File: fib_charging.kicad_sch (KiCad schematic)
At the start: 0 parts

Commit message: added several ICs, implementted schematics for charger, boost converter and LDOs
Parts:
- added C1, C12, C2, C3, C8: 0.1uF, symbol Device:C_Small
- added C10, C11, C13, C14, C15, C16, C17, C18, C19, C20, C4, C5, C9: 10uF, symbol Device:C_Small
- added C6, C7: 47nF, symbol Device:C_Small
- added D1, D2: BZT52Bxx, Diode_SMD:D_SOD-123F, symbol Diode:BZT52Bxx
- added D3: LED, symbol Device:LED
- added J5, J6: Conn_01x02, symbol Connector_Generic:Conn_01x02
- added L1: 1uH, symbol Device:L_Small
- added P2: USB_C_Plug_USB2.0, symbol Connector:USB_C_Plug_USB2.0
- added Q1, Q2, Q3, Q4: CSD17581Q3A, Package_SON:VSON-8_3.3x3.3mm_P0.65mm_NexFET, symbol Transistor_FET:CSD17581Q3A
- added R1, R2: 294R, symbol Device:R_Small
- added R10, R5: 127K, symbol Device:R_Small
- added R3: 10K, symbol Device:R_Small
- added R4: 6.04K, symbol Device:R_Small
- added R6: 100K, symbol Device:R_Small
- added R7: 100R, symbol Device:R_Small
- added R8: 5.24K, symbol Device:R_Small
- added R9: 30.31K, symbol Device:R_Small
- added TH1: 10K, symbol Device:Thermistor
- added U1: BQ25798RQMR, Fibel2:IBQ25798RQMR, symbol Fibel2:BQ25798RQMR
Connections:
- new net: D2.1 (K), Q3.4 (G), Q4.4 (G), R2.1
- new net: R2.2, U1.11 (ACDRV1)
- new net: C10.1, C11.1, C8.1, C9.1, U1.29 (PMID)
- new net: C20.1, U1.24 (SDRV)
- new net: R8.2, R9.2, TH1.1, U1.16 (TS)
- new net: D3.2 (A), R10.2
- new net: R4.1, U1.20 (PROG)
- new net: C3.1, C4.1, C5.1, Q2.5 (D), Q4.5 (D), U1.2 (VBUS), U1.3 (VBUS)
- new net: C1.1, J5.2 (Pin_2), Q1.5 (D), U1.8 (VAC2)
- new net: C18.1, C19.1, J6.1 (Pin_1), R7.1, U1.22 (BAT), U1.23 (BAT)
- new net: D2.2 (A), Q3.1 (S), Q3.2 (S), Q3.3 (S), Q4.1 (S), Q4.2 (S), Q4.3 (S)
- new net: D3.1 (K), U1.1 (STAT)
- new net: R1.2, U1.10 (ACDRV2)
- new net: R5.2, R6.1, U1.17 (ILIM_HIZ)
- new net: R7.2, U1.18 (BATP)
- new net: C7.2, U1.19 (BTST2)
- new net: C7.1, L1.1, U1.26 (SW2)
- new net: C6.2, L1.2, U1.28 (SW1)
- new net: C6.1, U1.4 (BTST1)
- new net: P2.A7 (D-), U1.6 (D+)
- new net: P2.A6 (D+), U1.7 (D-)
- new net: C2.1, P2.A4 (VBUS), P2.A9 (VBUS), P2.B4 (VBUS), P2.B9 (VBUS), Q3.5 (D), U1.9 (VAC1)
- new net: D1.1 (K), Q1.4 (G), Q2.4 (G), R1.1
- new net: D1.2 (A), Q1.1 (S), Q1.2 (S), Q1.3 (S), Q2.1 (S), Q2.2 (S), Q2.3 (S)
- new net: P2.A5 (CC), R3.2
- new net CHG_SCL: U1.14 (SCL)
- new net CHG_SDA: U1.15 (SDA)
- new net GND: C1.2, C10.2, C11.2, C12.2, C13.2, C14.2, C15.2, C16.2, C17.2, C18.2, C19.2, C2.2, C20.2, C3.2, C4.2, C5.2, C8.2, C9.2, J5.1 (Pin_1), J6.2 (Pin_2), P2.A1 (GND), P2.A12 (GND), P2.B1 (GND), P2.B12 (GND), P2.S1 (SHIELD), R3.1, R4.2, R6.2, R9.1, TH1.2, U1.27 (GND)
- new net REGN: R10.1, R5.1, R8.1, U1.5 (REGN)
- new net VCC: C12.1, C13.1, C14.1, C15.1, C16.1, C17.1, U1.25 (SYS)
- new net ~{CHG_CE}: U1.13 (~{CE})
- new net ~{CHG_INT}: U1.21 (~{INT})
- no-connect marks 0 -> 1
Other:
- note added: "BATT_CON"
- note added: "SOLAR_CON"

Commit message: added symbol&footprint for orin/sodimm, added a bunch of specs and docs, partially implemented audio, full steam ahead
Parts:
- C1, C10, C11, C12, C13, C14, C15, C16, C17, C18, C19, C2, C20, C3, C4, C5, C6, C7, C8, C9: footprint (none) -> Capacitor_SMD:C_0603_1608Metric
- J5, J6: footprint (none) -> Connector_JST:JST_EH_S2B-EH_1x02_P2.50mm_Horizontal
- R1, R10, R2, R3, R4, R5, R6, R7, R8, R9: footprint (none) -> Resistor_SMD:R_0603_1608Metric
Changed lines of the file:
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@@
 			)
 		)
-		(property "Footprint" ""
+		(property "Footprint" "Resistor_SMD:R_0603_1608Metric"
 			(at 83.82 67.31 0)
 			(effects
@@
 			)
 		)
-		(property "Footprint" ""
+		(property "Footprint" "Capacitor_SMD:C_0603_1608Metric"
 			(at 217.17 67.31 0)
 			(effects
@@
 			)
 		)
-		(property "Footprint" ""
+		(property "Footprint" "Capacitor_SMD:C_0603_1608Metric"
 			(at 196.85 67.31 0)
 			(effects
@@
 			)
 		)
-		(property "Footprint" ""
+		(property "Footprint" "Capacitor_SMD:C_0603_1608Metric"
 			(at 184.15 57.15 0)
 			(effects
@@
 			)
 		)
-		(property "Footprint" ""
+		(property "Footprint" "Resistor_SMD:R_0603_1608Metric"
 			(at 184.15 95.25 0)
 			(effects
@@
 			)
 		)
-		(property "Footprint" ""
+		(property "Footprint" "Resistor_SMD:R_0603_1608Metric"
 			(at 194.31 85.09 0)
 			(effects
@@
 			)
 		)
-		(property "Footprint" ""
+		(property "Footprint" "Resistor_SMD:R_0603_1608Metric"
 			(at 184.15 69.85 0)
 			(effects
@@
 			)
 		)
-		(property "Footprint" ""
+		(property "Footprint" "Capacitor_SMD:C_0603_1608Metric"
 			(at 109.22 49.53 0)
 			(effects
@@
 			)
 		)
-		(property "Footprint" ""
+		(property "Footprint" "Capacitor_SMD:C_0603_1608Metric"
 			(at 59.69 59.69 0)
 			(effects
@@
 			)
 		)
-		(property "Footprint" ""
+		(property "Footprint" "Connector_JST:JST_EH_S2B-EH_1x02_P2.50mm_Horizontal"
 			(at 228.6 49.53 0)
 			(effects
@@
 			)
 		)
-		(property "Footprint" ""
+		(property "Footprint" "Capacitor_SMD:C_0603_1608Metric"
 			(at 203.2 52.07 0)
 			(effects
@@
 			)
 		)
-		(property "Footprint" ""
+		(property "Footprint" "Capacitor_SMD:C_0603_1608Metric"
 			(at 246.38 92.71 0)
 			(effects
@@
 			)
 		)
-		(property "Footprint" ""
+		(property "Footprint" "Capacitor_SMD:C_0603_1608Metric"
 			(at 213.36 52.07 0)
 			(effects
@@
 			)
 		)
-		(property "Footprint" ""
+		(property "Footprint" "Capacitor_SMD:C_0603_1608Metric"
 			(at 129.54 49.53 0)
 			(effects
@@
 			)
 		)
-		(property "Footprint" ""
+		(property "Footprint" "Capacitor_SMD:C_0603_1608Metric"
 			(at 195.58 92.71 0)
 			(effects
@@
 			)
 		)
-		(property "Footprint" ""
+		(property "Footprint" "Capacitor_SMD:C_0603_1608Metric"
 			(at 226.06 92.71 0)
 			(effects
@@
 			)
 		)
-		(property "Footprint" ""
+		(property "Footprint" "Resistor_SMD:R_0603_1608Metric"
 			(at 54.61 88.9 0)
 			(effects
@@
 			)
 		)
-		(property "Footprint" ""
+		(property "Footprint" "Resistor_SMD:R_0603_1608Metric"
 			(at 186.69 78.74 0)
 			(effects
@@
 			)
 		)
-		(property "Footprint" ""
+		(property "Footprint" "Connector_JST:JST_EH_S2B-EH_1x02_P2.50mm_Horizontal"
 			(at 45.72 59.69 0)
 			(effects
@@
 			)
 		)
-		(property "Footprint" ""
+		(property "Footprint" "Capacitor_SMD:C_0603_1608Metric"
 			(at 119.38 49.53 0)
 			(effects
@@
 			)
 		)
-		(property "Footprint" ""
+		(property "Footprint" "Capacitor_SMD:C_0603_1608Metric"
 			(at 64.77 72.39 0)
 			(effects
@@
 			)
 		)
-		(property "Footprint" ""
+		(property "Footprint" "Capacitor_SMD:C_0603_1608Metric"
 			(at 125.73 95.25 0)
 			(effects
@@
 			)
 		)
-		(property "Footprint" ""
+		(property "Footprint" "Capacitor_SMD:C_0603_1608Metric"
 			(at 205.74 92.71 0)
 			(effects
@@
 			)
 		)
-		(property "Footprint" ""
+		(property "Footprint" "Resistor_SMD:R_0603_1608Metric"
 			(at 194.31 74.93 0)
 			(effects
@@
 			)
 		)
-		(property "Footprint" ""
+		(property "Footprint" "Capacitor_SMD:C_0603_1608Metric"
 			(at 236.22 92.71 0)
 			(effects
@@
 			)
 		)
-		(property "Footprint" ""
+		(property "Footprint" "Capacitor_SMD:C_0603_1608Metric"
 			(at 125.73 85.09 0)
 			(effects
@@
 			)
 		)
-		(property "Footprint" ""
+		(property "Footprint" "Capacitor_SMD:C_0603_1608Metric"
 			(at 207.01 67.31 0)
 			(effects
@@
 			)
 		)
-		(property "Footprint" ""
+		(property "Footprint" "Capacitor_SMD:C_0603_1608Metric"
 			(at 227.33 67.31 0)
 			(effects
@@
 			)
 		)
-		(property "Footprint" ""
+		(property "Footprint" "Capacitor_SMD:C_0603_1608Metric"
 			(at 215.9 92.71 0)
 			(effects
@@
 			)
 		)
-		(property "Footprint" ""
+		(property "Footprint" "Resistor_SMD:R_0603_1608Metric"
 			(at 185.42 52.07 0)
 			(effects
@@
 			)
 		)
-		(property "Footprint" ""
+		(property "Footprint" "Resistor_SMD:R_0603_1608Metric"
 			(at 184.15 102.87 0)
 			(effects
@@
 			)
 		)
-		(property "Footprint" ""
+		(property "Footprint" "Resistor_SMD:R_0603_1608Metric"
 			(at 83.82 59.69 0)
 			(effects

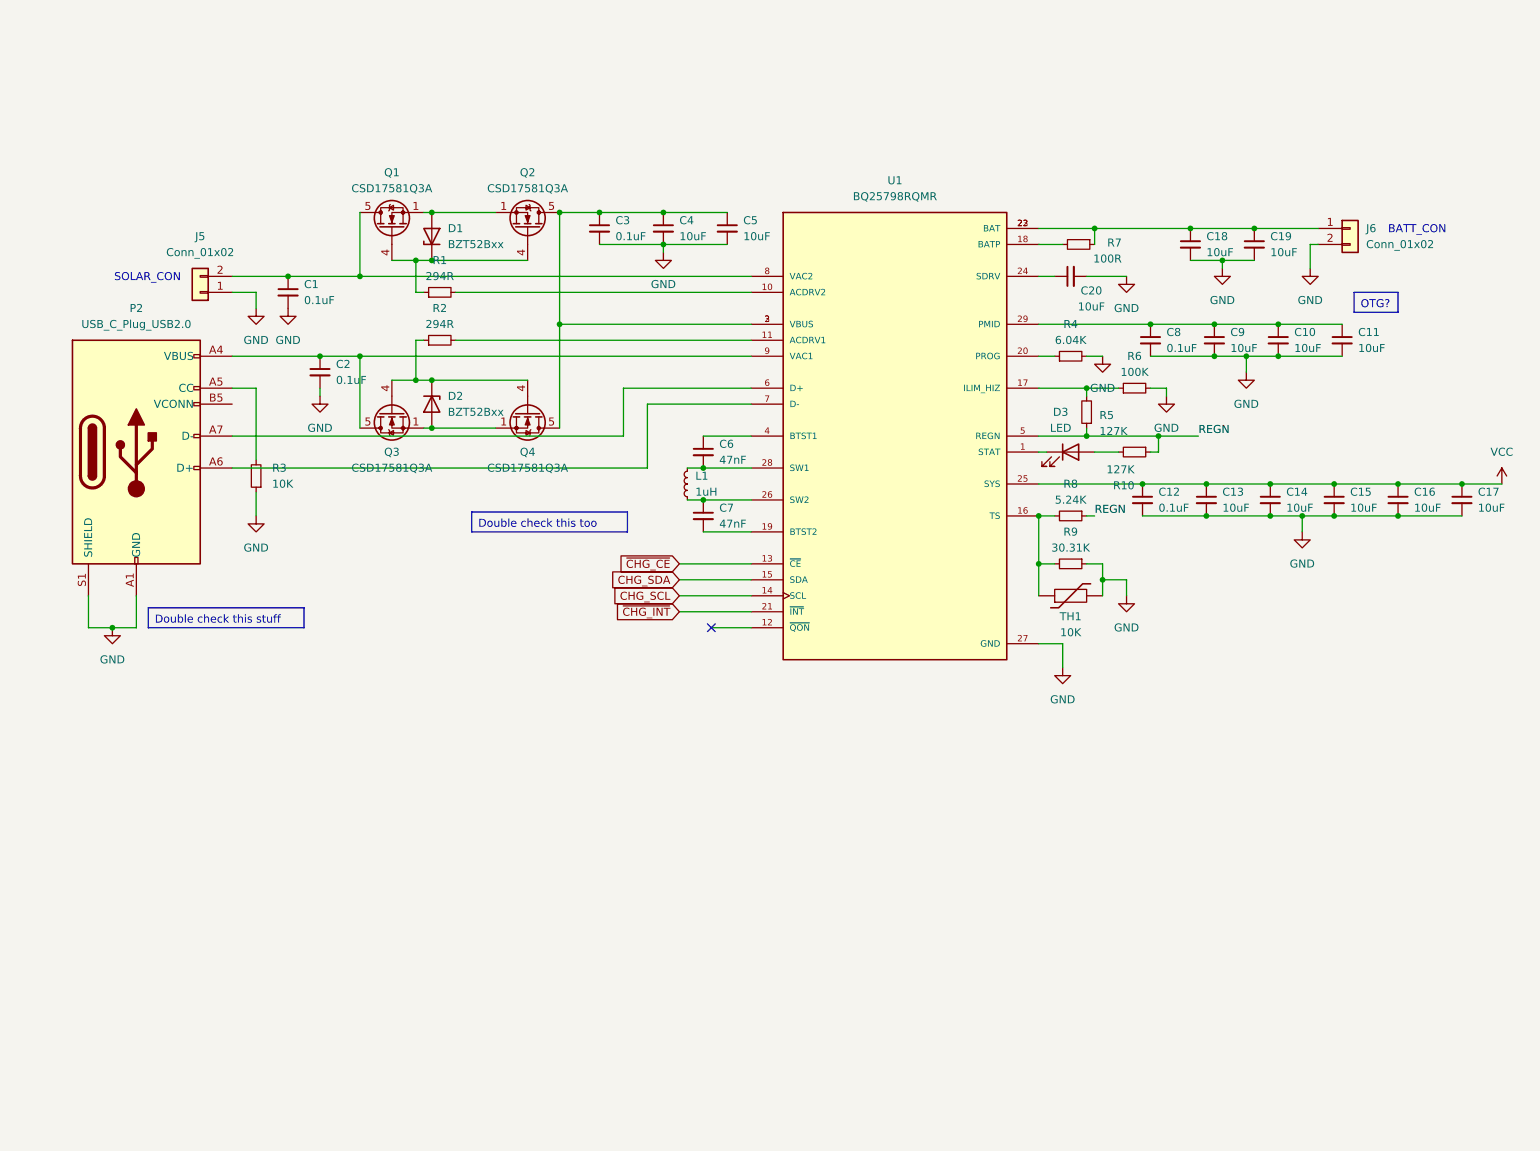
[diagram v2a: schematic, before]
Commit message: added usb+PD+DP & pcie implementations from antmicro design, added specs for USB components, rethought power+usb arch
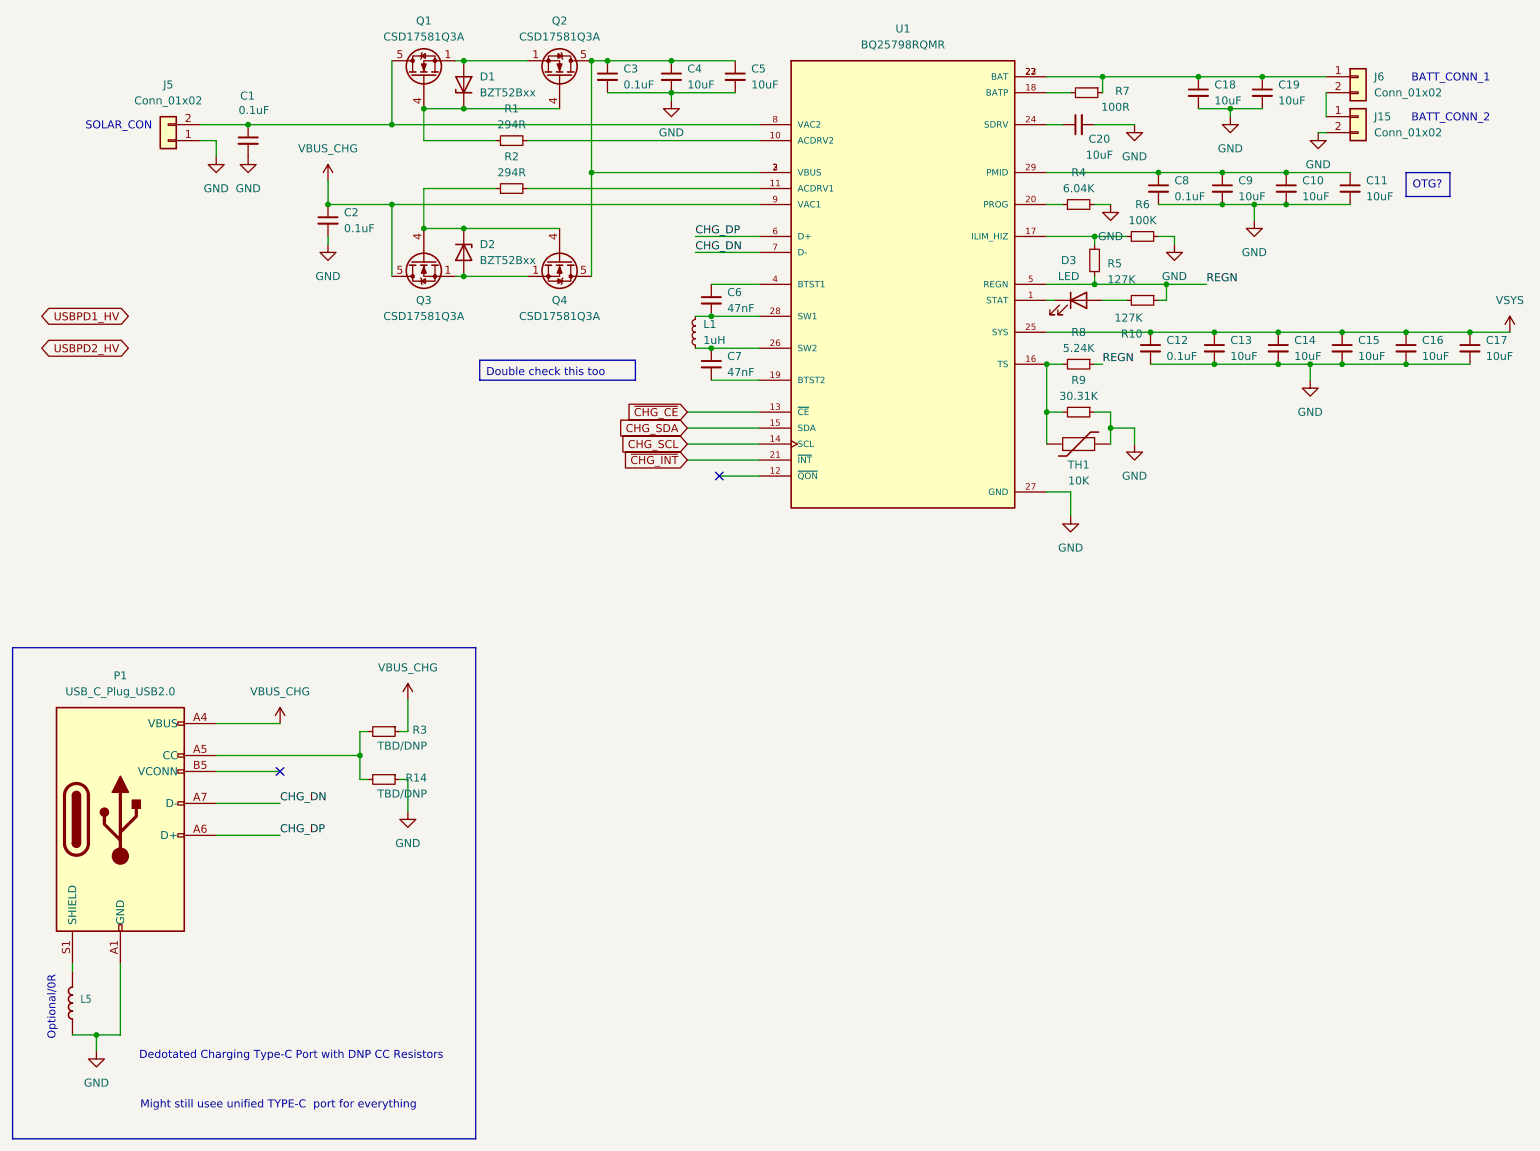
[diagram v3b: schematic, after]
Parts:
- removed P2: USB_C_Plug_USB2.0, symbol Connector:USB_C_Plug_USB2.0
- added J15: Conn_01x02, Connector_JST:JST_EH_S2B-EH_1x02_P2.50mm_Horizontal, symbol Connector_Generic:Conn_01x02
- added L5: ~, Untitled:L0603, symbol Untitled-eagle-import:INDUCTOR/FERRITE-BEAD'0603'
- added P1: USB_C_Plug_USB2.0, symbol Connector:USB_C_Plug_USB2.0
- added R14: TBD/DNP, Resistor_SMD:R_0603_1608Metric, symbol Device:R_Small
- R3: value 10K -> TBD/DNP
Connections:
- net GND: now also J15.2 (Pin_2), L5.1, P1.A1 (GND), P1.A12 (GND), P1.B1 (GND), P1.B12 (GND), R14.1; no longer J6.2 (Pin_2), R3.1
- net CHG_DP: now reaches U1.6 (D+)
- net CHG_DP: now also P1.A6 (D+)
- net CHG_DN: now reaches U1.7 (D-)
- net CHG_DN: now also P1.A7 (D-)
- net VBUS_CHG: now reaches C2.1, Q3.5 (D), U1.9 (VAC1)
- net VBUS_CHG: now also R3.1, P1.A4 (VBUS), P1.A9 (VBUS), P1.B4 (VBUS), P1.B9 (VBUS)
- net at R3.2: now also P1.A5 (CC), R14.2
- net VCC renamed VSYS
- new net: J15.1 (Pin_1), J6.2 (Pin_2)
- new net: L5.2, P1.S1 (SHIELD)
- no-connect marks 1 -> 2
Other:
- note added: "BATT_CONN_1"
- note added: "BATT_CONN_2"
- note added: "Dedotated Charging Type-C Port with DNP CC Resistors"
- note added: "Might still usee unified TYPE-C port for everything"
- note added: "Optional/0R"
- note removed: "BATT_CON"
- moved on the sheet: C1, C10, C11, C12, C13, C14, C15, C16, C17, C18, C19, C2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

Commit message: added nets for 40 pin headers (epd & rpi header) connected some of the nets i'm reeusing
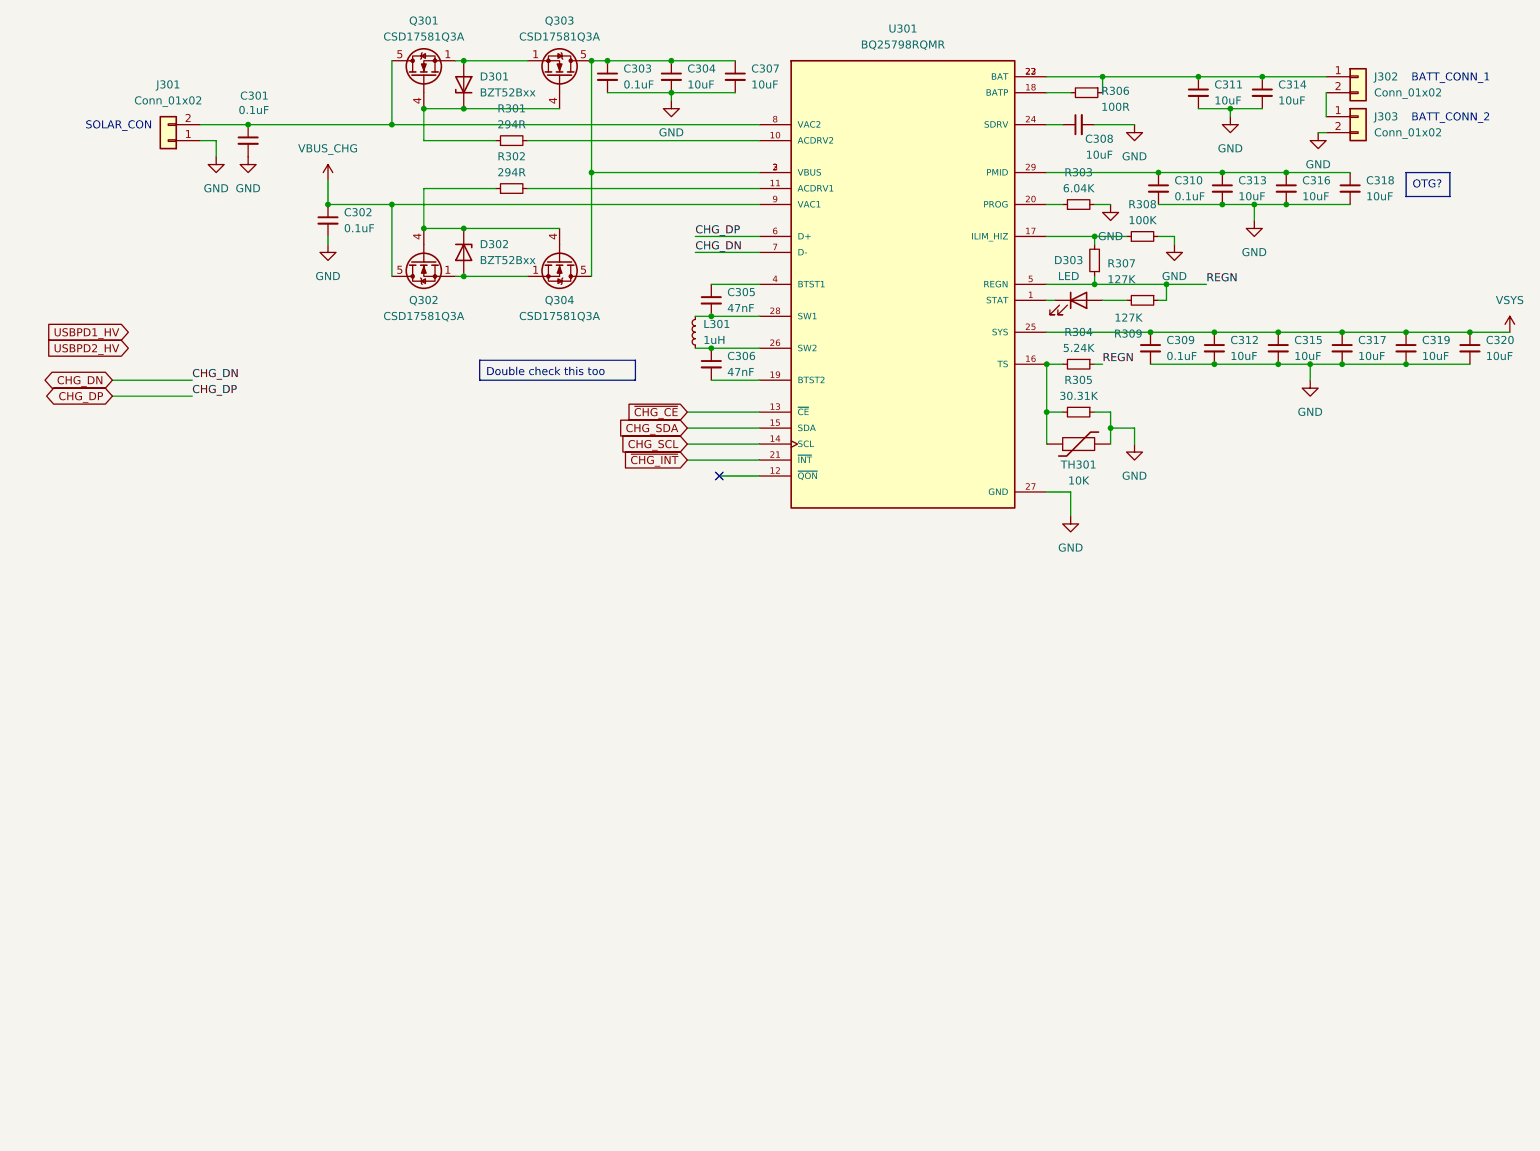
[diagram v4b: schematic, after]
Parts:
- removed L5: ~, Untitled:L0603, symbol Untitled-eagle-import:INDUCTOR/FERRITE-BEAD'0603'
- removed P1: USB_C_Plug_USB2.0, symbol Connector:USB_C_Plug_USB2.0
- removed R14, R3: TBD/DNP, Resistor_SMD:R_0603_1608Metric, symbol Device:R_Small
- D303: renamed from D3; footprint (none) -> Capacitor_SMD:C_0603_1608Metric
- L301: renamed from L1; footprint (none) -> Resistor_SMD:R_0603_1608Metric
- TH301: renamed from TH1; footprint (none) -> Resistor_SMD:R_0603_1608Metric
- renumbered C1 to C301, C2 to C302, C3 to C303, C4 to C304, C6 to C305, C7 to C306, C5 to C307, C20 to C308, C12 to C309, C8 to C310, C18 to C311, C13 to C312, C9 to C313, C19 to C314, C14 to C315, C10 to C316, C15 to C317, C11 to C318, C16 to C319, C17 to C320, D1 to D301, D2 to D302, J5 to J301, J6 to J302, J15 to J303, Q1 to Q301, Q3 to Q302, Q2 to Q303, Q4 to Q304, R1 to R301, R2 to R302, R4 to R303, R8 to R304, R9 to R305, R7 to R306, R5 to R307, R6 to R308, R10 to R309, U1 to U301
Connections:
- no-connect marks 2 -> 1
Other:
- note removed: "Dedotated Charging Type-C Port with DNP CC Resistors"
- note removed: "Might still usee unified TYPE-C port for everything"
- note removed: "Optional/0R"
